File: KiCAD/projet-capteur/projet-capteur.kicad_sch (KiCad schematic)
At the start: 20 parts, among them J1 Power, J2 Analog, J3 Digital/PWM, J4 Digital/PWM, U2 LTC1050

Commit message: Seance Realisation du shield 12.03 v2
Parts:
- removed R3: 1k, Resistor_THT:R_Axial_DIN0207_L6.3mm_D2.5mm_P5.08mm_Vertical, symbol Device:R
- added C4: C, Capacitor_THT:C_Disc_D6.0mm_W2.5mm_P5.00mm, symbol Device:C
- added CG1: ~, MyLibEmpreinte:Capteur Graphene, symbol MyLibGraphite:Capteur
- R6: value R -> 10k
- ROE1: footprint MyLibEmpreinte:Rotary Encoder -> MyLibEmpreinte:RotaryEncoder
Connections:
- net *6 is gone; now on net ROE 3: J4.2 (Pin_2)
- net 4 is gone; now on net ROE 4: J4.4 (Pin_4)
- net 7 is gone; now on net RX: J4.1 (Pin_1)
- net A1 is gone; now on net Sortie Flex: J2.2 (Pin_2)
- net *3: no longer U3.4 (Tx)
- net 5V: now also ROE1.2 (Vcc), CG1.1 (Vcc)
- net GND: now also MCP1.6 (P0W), MCP1.7 (P0B), ROE1.1 (GND), C4.1
- net Sortie Capteur: now also CG1.2 (Sortie)
- net Sortie Flex: now reaches FS1.1 (FlexPin), R6.1
- net R3: now reaches C2.1, R4.1, U2.3 (+)
- net R3: now also MCP1.5 (P0A)
- net ROE 3: now reaches ROE1.3 (SW)
- net ROE 4: now reaches ROE1.4 (DT)
- net ROE 5: now reaches ROE1.5 (CLK)
- net ROE 5: now also J4.6 (Pin_6), C4.2
- net 2 renamed RX
- net RX: no longer J4.6 (Pin_6)
- net 8 renamed TX
- net TX: now also U3.4 (Tx)
- no-connect marks 3 -> 7
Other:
- moved on the sheet: C1, C2, C3, R1, R2, R4, R5, ROE1, U2

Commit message: Seance Realisation du shield 13.03
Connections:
- net R3: now also U2.2 (-); no longer U2.3 (+)
- net at C1.1, R1.2, R2.1: now also U2.3 (+); no longer U2.2 (-)
- no-connect marks 7 -> 13
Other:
- moved on the sheet: U3
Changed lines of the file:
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@@
 	)
 	(junction
+		(at 34.29 73.66)
+		(diameter 0)
+		(color 0 0 0 0)
+	)
+	(junction
 		(at 48.26 153.67)
 		(diameter 0)
@@
 	)
 	(junction
-		(at 34.29 73.66)
-		(diameter 0)
-		(color 0 0 0 0)
-	)
-	(junction
 		(at 215.9 68.58)
 		(diameter 0)
@@
 	)
 	(no_connect
+		(at 82.55 27.94)
+	)
+	(no_connect
+		(at 24.13 81.28)
+	)
+	(no_connect
 		(at 82.55 81.28)
 	)
 	(no_connect
-		(at 99.06 92.71)
+		(at 82.55 33.02)
+	)
+	(no_connect
+		(at 107.95 118.11)
+	)
+	(no_connect
+		(at 82.55 30.48)
 	)
 	(no_connect
@@
 	)
 	(no_connect
-		(at 99.06 73.66)
+		(at 82.55 40.64)
+	)
+	(no_connect
+		(at 107.95 99.06)
 	)
 	(no_connect
@@
 		(at 82.55 86.36)
 	)
+	(no_connect
+		(at 24.13 78.74)
+	)
 	(wire
 		(pts
@@
 	(wire
 		(pts
-			(xy 34.29 73.66) (xy 26.67 73.66)
-		)
-		(stroke
-			(width 0)
-			(type solid)
-		)
-	)
-	(wire
-		(pts
-			(xy 67.31 27.94) (xy 80.01 27.94)
+			(xy 67.31 27.94) (xy 82.55 27.94)
 		)
 		(stroke
@@
 	(wire
 		(pts
-			(xy 67.31 40.64) (xy 80.01 40.64)
+			(xy 67.31 40.64) (xy 82.55 40.64)
 		)
 		(stroke
@@
 	(wire
 		(pts
+			(xy 26.67 73.66) (xy 34.29 73.66)
+		)
+		(stroke
+			(width 0)
+			(type default)
+		)
+	)
+	(wire
+		(pts
+			(xy 24.13 81.28) (xy 39.37 81.28)
+		)
+		(stroke
+			(width 0)
+			(type default)
+		)
+	)
+	(wire
+		(pts
 			(xy 128.27 64.77) (xy 128.27 45.72)
 		)
@@
 	(wire
 		(pts
-			(xy 99.06 77.47) (xy 96.52 77.47)
+			(xy 107.95 102.87) (xy 105.41 102.87)
 		)
 		(stroke
@@
 	(wire
 		(pts
-			(xy 67.31 33.02) (xy 80.01 33.02)
+			(xy 67.31 33.02) (xy 82.55 33.02)
 		)
 		(stroke
@@
 	(wire
 		(pts
-			(xy 39.37 78.74) (xy 26.67 78.74)
-		)
-		(stroke
-			(width 0)
-			(type solid)
-		)
-	)
-	(wire
-		(pts
 			(xy 24.13 38.1) (xy 39.37 38.1)
 		)
@@
 	(wire
 		(pts
-			(xy 99.06 81.28) (xy 96.52 81.28)
+			(xy 107.95 106.68) (xy 105.41 106.68)
 		)
 		(stroke
@@
 	(wire
 		(pts
-			(xy 26.67 81.28) (xy 39.37 81.28)
-		)
-		(stroke
-			(width 0)
-			(type solid)
-		)
-	)
-	(wire
-		(pts
 			(xy 147.32 151.13) (xy 147.32 157.48)
 		)
@@
 	(wire
 		(pts
-			(xy 67.31 30.48) (xy 80.01 30.48)
+			(xy 24.13 78.74) (xy 39.37 78.74)
+		)
+		(stroke
+			(width 0)
+			(type solid)
+		)
+	)
+	(wire
+		(pts
+			(xy 67.31 30.48) (xy 82.55 30.48)
 		)
 		(stroke
@@
 	)
 	(global_label "RX"
-		(shape input)
+		(shape bidirectional)
 		(at 82.55 71.12 0)
 		(fields_autoplaced yes)
@@
 		)
 		(property "Intersheetrefs" "${INTERSHEET_REFS}"
-			(at 88.1098 71.12 0)
+			(at 89.1258 71.12 0)
 			(effects
 				(font
@@
 	)
 	(global_label "TX"
-		(shape input)
-		(at 99.06 85.09 180)
+		(shape bidirectional)
+		(at 107.95 110.49 180)
 		(fields_autoplaced yes)
 		(effects
@@
 		)
 		(property "Intersheetrefs" "${INTERSHEET_REFS}"
-			(at 93.8026 85.09 0)
+			(at 101.6766 110.49 0)
 			(effects
 				(font
@@
 	)
 	(global_label "RX"
-		(shape input)
-		(at 99.06 88.9 180)
+		(shape bidirectional)
+		(at 107.95 114.3 180)
 		(fields_autoplaced yes)
 		(effects
@@
 		)
 		(property "Intersheetrefs" "${INTERSHEET_REFS}"
-			(at 93.5002 88.9 0)
+			(at 101.3742 114.3 0)
 			(effects
 				(font
@@
 	(global_label "5V"
 		(shape bidirectional)
-		(at 96.52 77.47 180)
+		(at 105.41 102.87 180)
 		(fields_autoplaced yes)
 		(effects
@@
 		)
 		(property "Intersheetrefs" "${INTERSHEET_REFS}"
-			(at 90.1256 77.47 0)
+			(at 99.0156 102.87 0)
 			(effects
 				(font
@@
 	)
 	(global_label "TX"
-		(shape input)
+		(shape bidirectional)
 		(at 82.55 50.8 0)
 		(fields_autoplaced yes)
@@
 		)
 		(property "Intersheetrefs" "${INTERSHEET_REFS}"
-			(at 87.8074 50.8 0)
+			(at 88.8234 50.8 0)
 			(effects
 				(font
@@
 		(lib_name "GND_2")
 		(lib_id "power:GND")
-		(at 96.52 81.28 270)
+		(at 105.41 106.68 270)
 		(unit 1)
 		(exclude_from_sim no)
@@
 		(fields_autoplaced yes)
 		(property "Reference" "#PWR1"
-			(at 90.17 81.28 0)
+			(at 99.06 106.68 0)
 			(effects
 				(font
@@
 		)
 		(property "Value" "GND"
-			(at 91.44 81.28 0)
+			(at 100.33 106.68 0)
 			(effects
 				(font
@@
 		)
 		(property "Footprint" ""
-			(at 96.52 81.28 0)
+			(at 105.41 106.68 0)
 			(effects
 				(font
@@
 		)
 		(property "Datasheet" ""
-			(at 96.52 81.28 0)
+			(at 105.41 106.68 0)
 			(effects
 				(font
@@
 		)
 		(property "Description" "Power symbol creates a global label with name \"GND\" , ground"
-			(at 96.52 81.28 0)
+			(at 105.41 106.68 0)
 			(effects
 				(font
@@
 			)
 		)
-		(pin "4"
+		(pin "7"
 		)
 		(pin "2"
 		)
-		(pin "6"
+		(pin "4"
 		)
 		(pin "3"
 		)
-		(pin "7"
+		(pin "6"
+		)
+		(pin "1"
+		)
+		(pin "8"
+		)
+		(pin "5"
 		)
 		(instances
@@
 	(symbol
 		(lib_id "MyLibGraphite:HC-05_Bluetooth")
-		(at 105.41 83.82 270)
+		(at 114.3 109.22 270)
 		(unit 1)
 		(exclude_from_sim no)
@@
 		(fields_autoplaced yes)
 		(property "Reference" "U3"
-			(at 108.5851 97.79 0)
+			(at 117.4751 123.19 0)
 			(effects
 				(font
@@
 		)
 		(property "Value" "~"
-			(at 106.68 97.79 0)
+			(at 115.57 123.19 0)
 			(effects
 				(font
@@
 		)
 		(property "Footprint" "MyLibEmpreinte:HC-05"
-			(at 102.87 85.09 0)
+			(at 111.76 110.49 0)
 			(effects
 				(font
@@
 		)
 		(property "Datasheet" ""
-			(at 102.87 85.09 0)
+			(at 111.76 110.49 0)
 			(effects
 				(font
@@
 		)
 		(property "Description" ""
-			(at 102.87 85.09 0)
+			(at 111.76 110.49 0)
 			(effects
 				(font

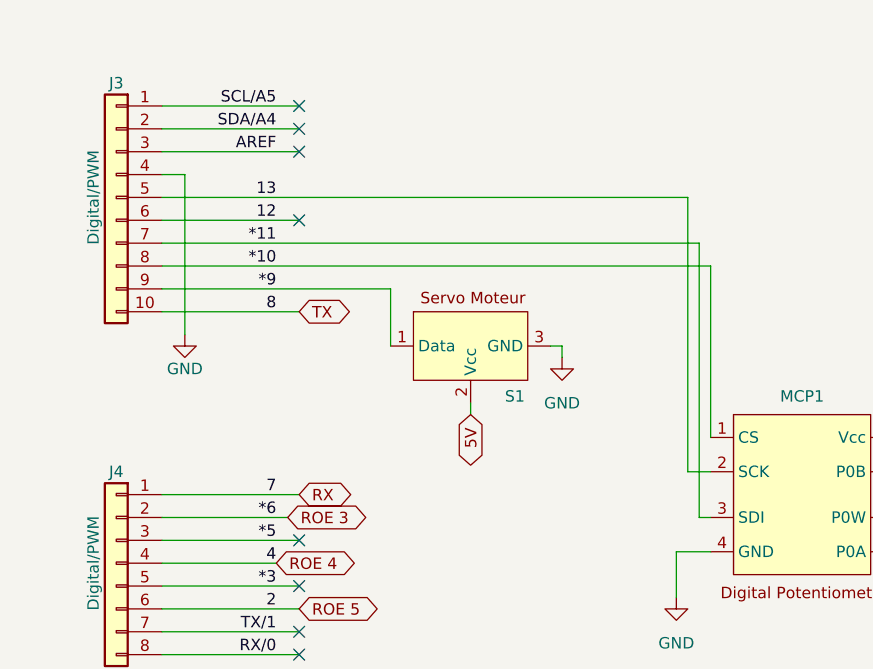
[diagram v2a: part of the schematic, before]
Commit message: Modif des tracks + pins
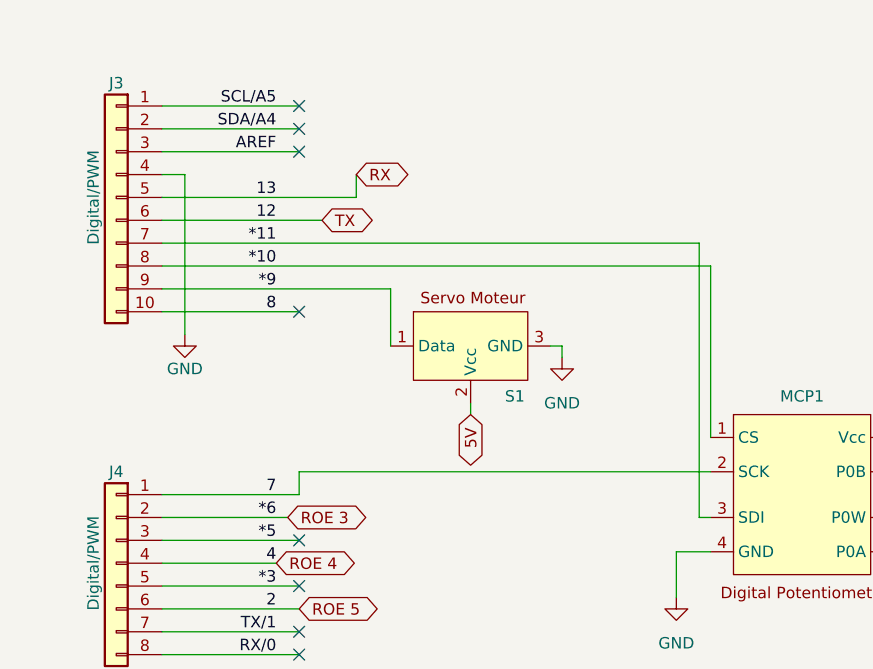
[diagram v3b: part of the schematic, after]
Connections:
- net 12 is gone; now on net TX: J3.6 (Pin_6)
- net RX: now also J3.5 (Pin_5); no longer J4.1 (Pin_1)
- net TX: no longer J3.10 (Pin_10)
- net 13 renamed 7
- net 7: now also J4.1 (Pin_1); no longer J3.5 (Pin_5)
- new net 8: J3.10 (Pin_10)
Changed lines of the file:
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@@
 	)
 	(no_connect
-		(at 82.55 40.64)
+		(at 82.55 50.8)
 	)
 	(no_connect
@@
 	(wire
 		(pts
-			(xy 125.73 68.58) (xy 128.27 68.58)
-		)
-		(stroke
-			(width 0)
-			(type solid)
-		)
-	)
-	(wire
-		(pts
 			(xy 121.92 132.08) (xy 121.92 137.16)
 		)
@@
 	(wire
 		(pts
-			(xy 67.31 38.1) (xy 125.73 38.1)
+			(xy 67.31 38.1) (xy 88.9 38.1)
 		)
 		(stroke
@@
 	(wire
 		(pts
-			(xy 67.31 40.64) (xy 82.55 40.64)
+			(xy 67.31 40.64) (xy 85.09 40.64)
 		)
 		(stroke
@@
 	(wire
 		(pts
+			(xy 82.55 68.58) (xy 128.27 68.58)
+		)
+		(stroke
+			(width 0)
+			(type solid)
+		)
+	)
+	(wire
+		(pts
 			(xy 107.95 102.87) (xy 105.41 102.87)
 		)
@@
 	(wire
 		(pts
-			(xy 125.73 38.1) (xy 125.73 68.58)
-		)
-		(stroke
-			(width 0)
-			(type solid)
-		)
-	)
-	(wire
-		(pts
 			(xy 77.47 148.59) (xy 77.47 132.08)
 		)
@@
 	(wire
 		(pts
+			(xy 88.9 35.56) (xy 88.9 38.1)
+		)
+		(stroke
+			(width 0)
+			(type default)
+		)
+	)
+	(wire
+		(pts
 			(xy 147.32 151.13) (xy 147.32 157.48)
 		)
@@
 			(width 0)
 			(type default)
+		)
+	)
+	(wire
+		(pts
+			(xy 82.55 68.58) (xy 82.55 71.12)
+		)
+		(stroke
+			(width 0)
+			(type solid)
 		)
 	)
@@
 		)
 	)
+	(global_label "5V"
+		(shape bidirectional)
+		(at 34.29 25.4 90)
+		(fields_autoplaced yes)
+		(effects
+			(font
+				(size 1.27 1.27)
+			)
+			(justify left)
+		)
+		(property "Intersheetrefs" "${INTERSHEET_REFS}"
+			(at 34.29 19.0056 90)
+			(effects
+				(font
+					(size 1.27 1.27)
+				)
+				(justify left)
+				(hide yes)
+			)
+		)
+	)
 	(global_label "RX"
 		(shape bidirectional)
-		(at 82.55 71.12 0)
+		(at 88.9 35.56 0)
 		(fields_autoplaced yes)
 		(effects
@@
 		)
 		(property "Intersheetrefs" "${INTERSHEET_REFS}"
-			(at 89.1258 71.12 0)
-			(effects
-				(font
-					(size 1.27 1.27)
-				)
-				(justify left)
-				(hide yes)
-			)
-		)
-	)
-	(global_label "5V"
-		(shape bidirectional)
-		(at 34.29 25.4 90)
-		(fields_autoplaced yes)
-		(effects
-			(font
-				(size 1.27 1.27)
-			)
-			(justify left)
-		)
-		(property "Intersheetrefs" "${INTERSHEET_REFS}"
-			(at 34.29 19.0056 90)
+			(at 95.4758 35.56 0)
 			(effects
 				(font
@@
 		)
 	)
+	(global_label "TX"
+		(shape bidirectional)
+		(at 85.09 40.64 0)
+		(fields_autoplaced yes)
+		(effects
+			(font
+				(size 1.27 1.27)
+			)
+			(justify left)
+		)
+		(property "Intersheetrefs" "${INTERSHEET_REFS}"
+			(at 91.3634 40.64 0)
+			(effects
+				(font
+					(size 1.27 1.27)
+				)
+				(justify left)
+				(hide yes)
+			)
+		)
+	)
 	(global_label "Sortie Capteur"
 		(shape input)
@@
 				(hide yes)
 			)
-		)
-	)
-	(global_label "TX"
-		(shape bidirectional)
-		(at 82.55 50.8 0)
-		(fields_autoplaced yes)
-		(effects
-			(font
-				(size 1.27 1.27)
-			)
-			(justify left)
-		)
-		(property "Intersheetrefs" "${INTERSHEET_REFS}"
-			(at 88.8234 50.8 0)
-			(effects
-				(font
-					(size 1.27 1.27)
-				)
-				(justify left)
-				(hide yes)
-			)

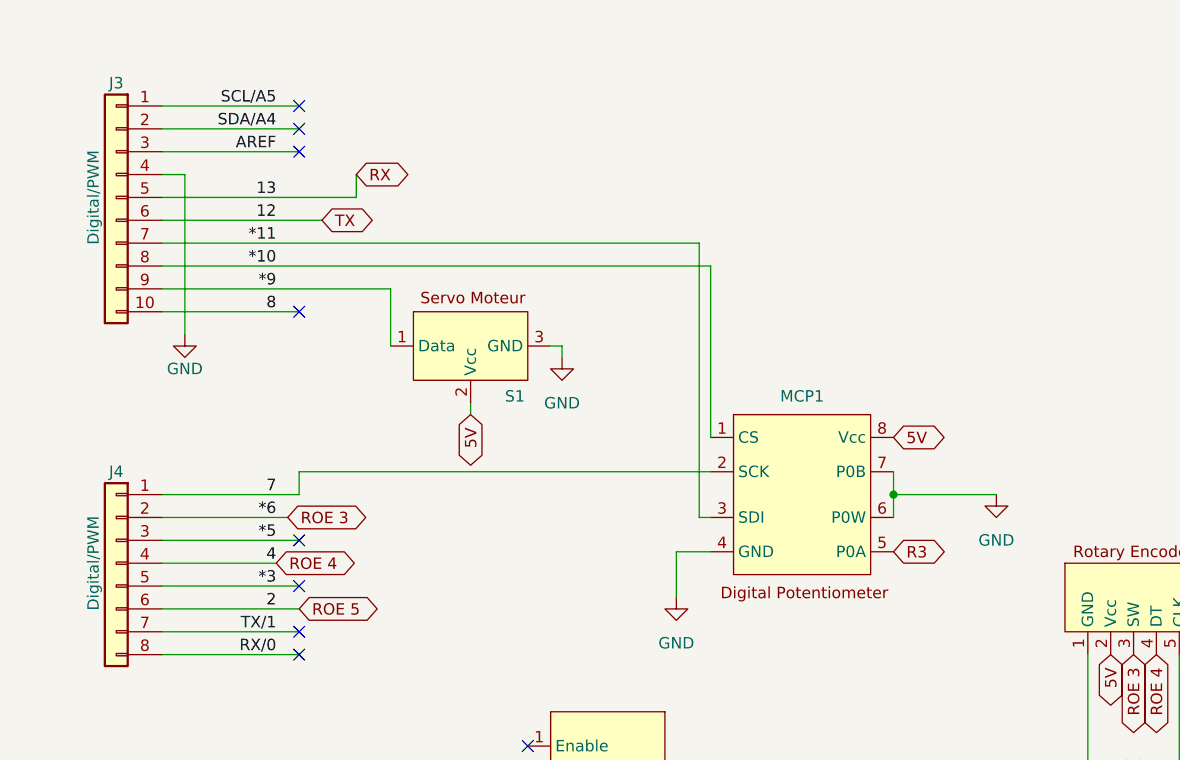
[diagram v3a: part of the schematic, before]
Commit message: Reparation des pins du potentiometre
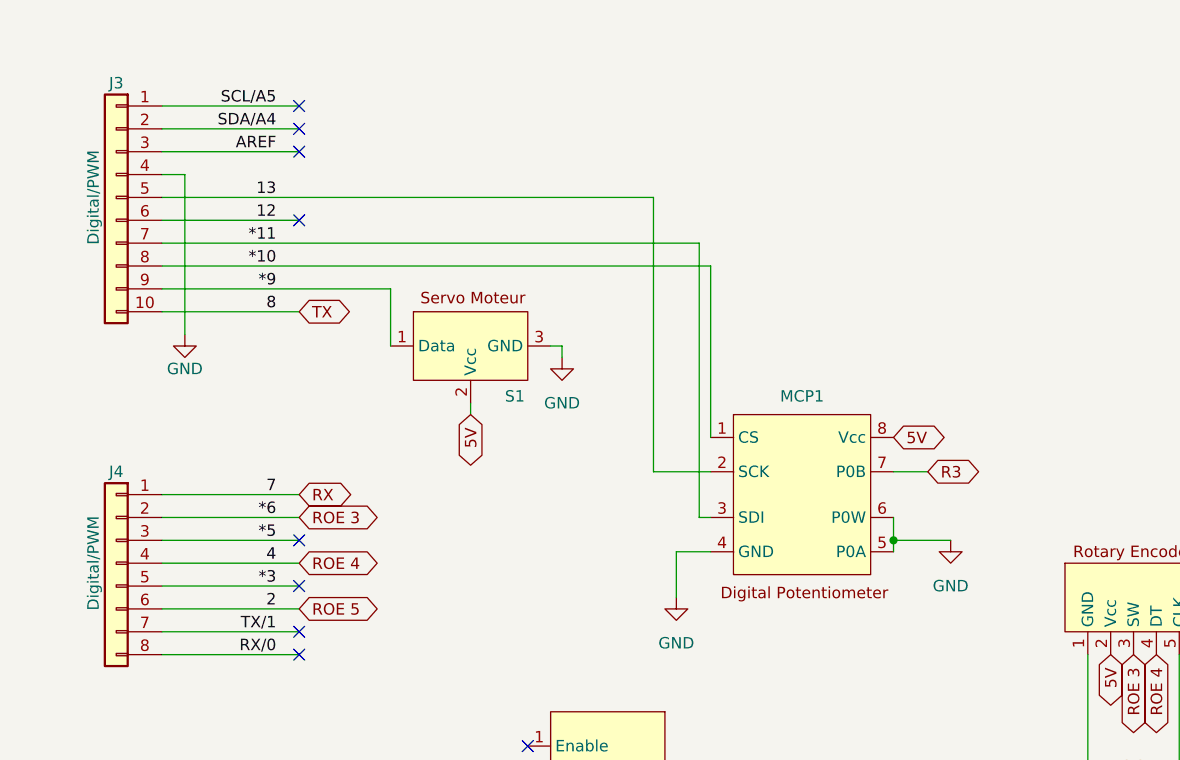
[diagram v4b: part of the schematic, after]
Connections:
- net 8 is gone; now on net TX: J3.10 (Pin_10)
- net GND: now also MCP1.5 (P0A); no longer MCP1.7 (P0B)
- net R3: now also MCP1.7 (P0B); no longer MCP1.5 (P0A)
- net RX: now also J4.1 (Pin_1); no longer J3.5 (Pin_5)
- net TX: no longer J3.6 (Pin_6)
- net 7 renamed 13
- net 13: now also J3.5 (Pin_5); no longer J4.1 (Pin_1)
- new net 12: J3.6 (Pin_6)
